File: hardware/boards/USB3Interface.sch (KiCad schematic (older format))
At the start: 5 parts, among them J2 USB3_Micro_B_Amphenol, U1 ECP5UM5G-381caBGA, U3 CYUSB3014

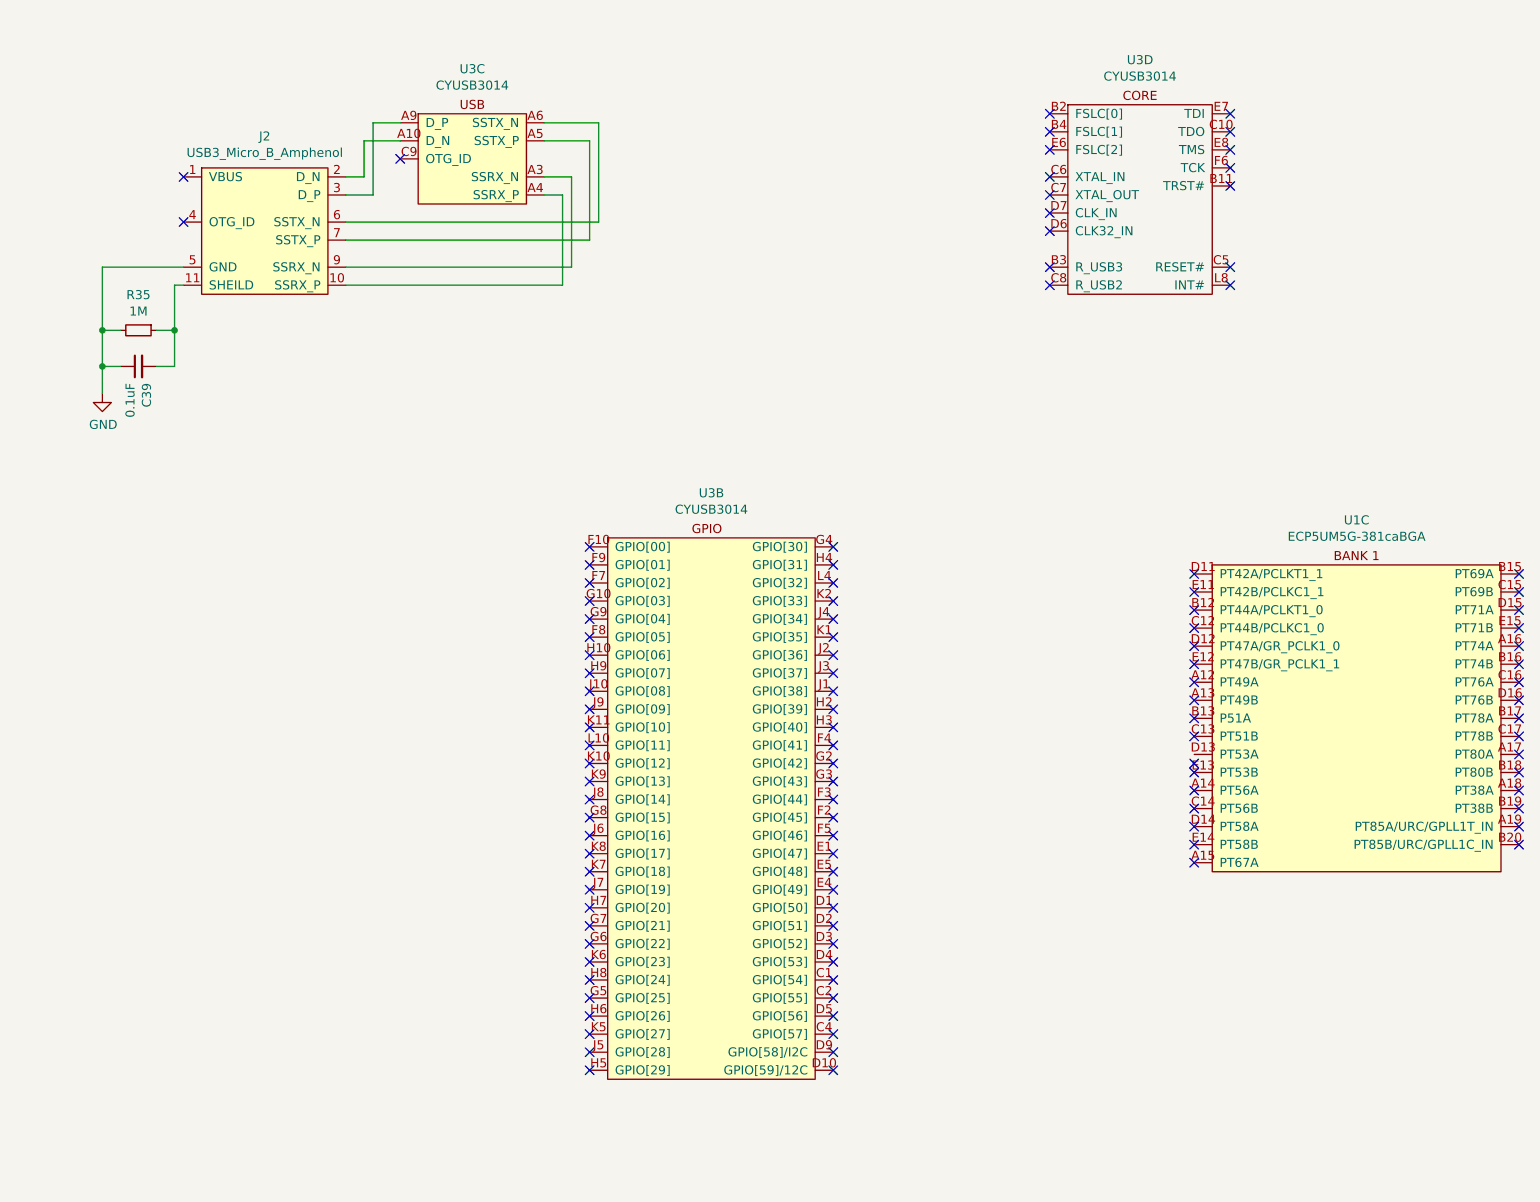
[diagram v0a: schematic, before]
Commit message: In an AHDH fuled stupor I made a bunch of changes, only the last of which I recall, which would be adding fiducials
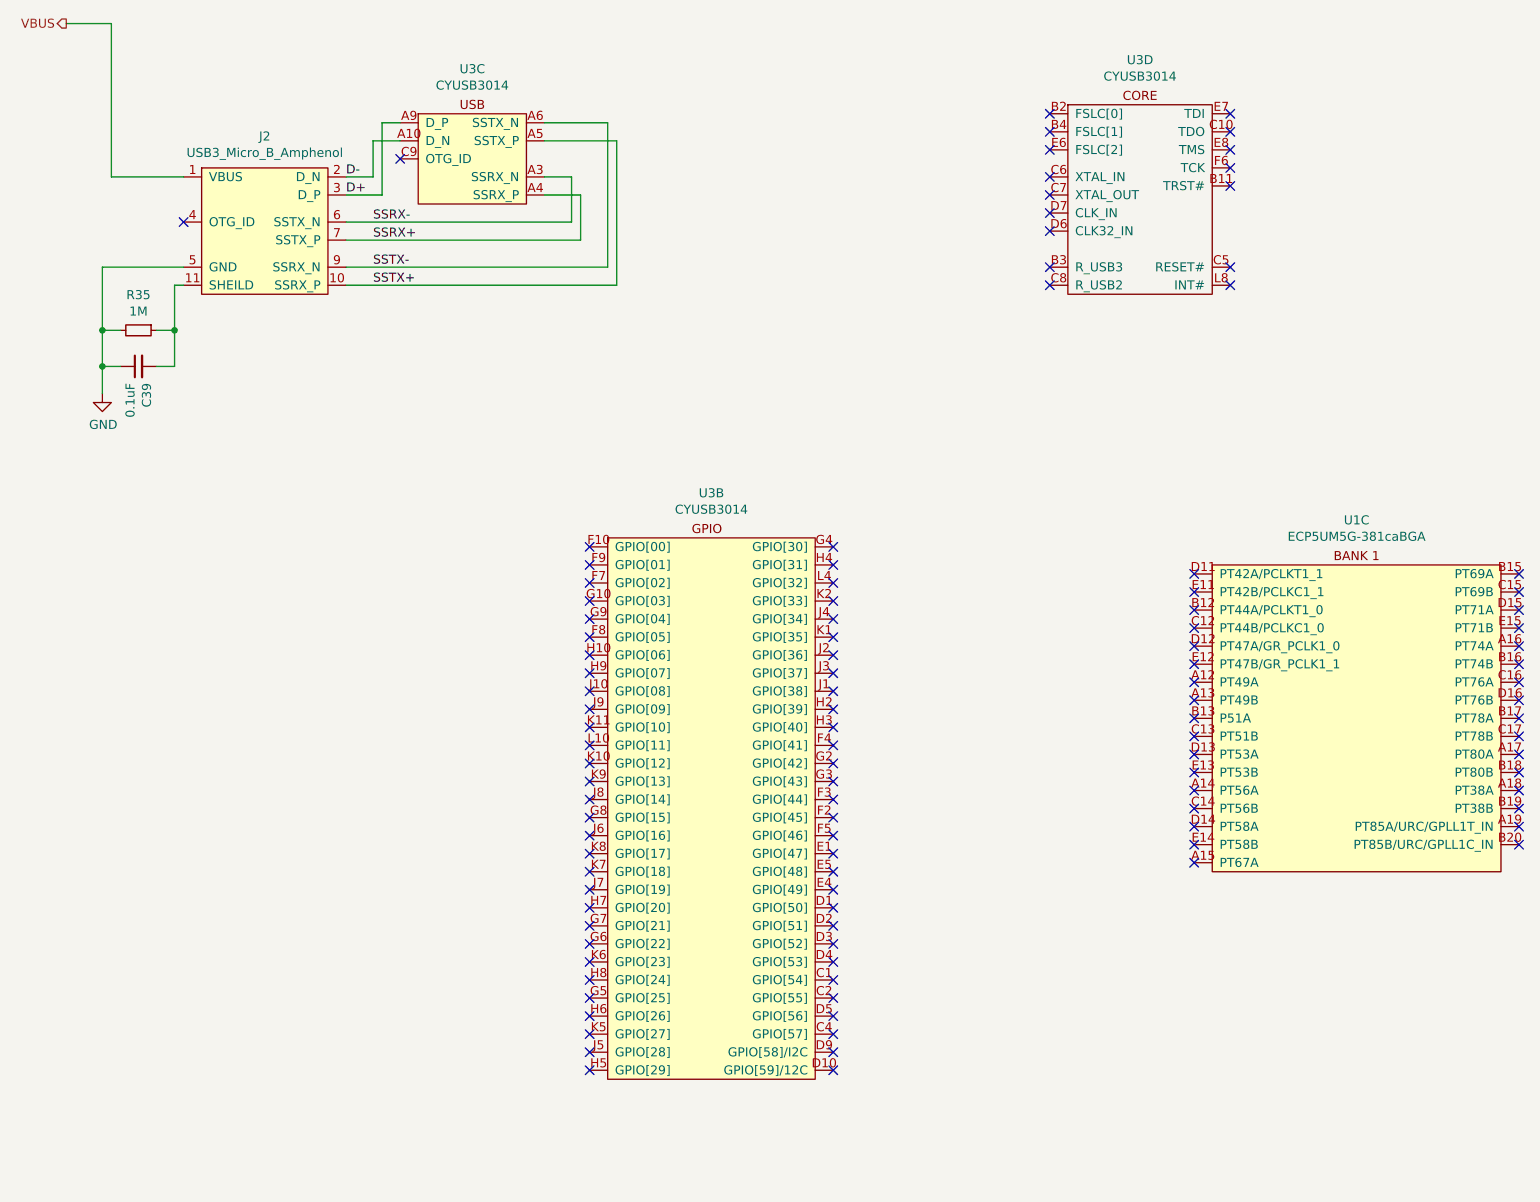
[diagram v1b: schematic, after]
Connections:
- net D-: now reaches J2.2 (D_N), U3.A10 (D_N)
- net SSRX-: now reaches U3.A3 (SSRX_N)
- net SSRX-: now also J2.6 (SSTX_N); no longer J2.9 (SSRX_N)
- net SSRX+: now reaches U3.A4 (SSRX_P)
- net SSRX+: now also J2.7 (SSTX_P); no longer J2.10 (SSRX_P)
- net SSTX+: now reaches U3.A5 (SSTX_P)
- net SSTX+: now also J2.10 (SSRX_P); no longer J2.7 (SSTX_P)
- net SSTX-: now reaches U3.A6 (SSTX_N)
- net SSTX-: now also J2.9 (SSRX_N); no longer J2.6 (SSTX_N)
- net D+: now reaches J2.3 (D_P), U3.A9 (D_P)
- net VBUS: now reaches J2.1 (VBUS)
- no-connect marks 112 -> 111
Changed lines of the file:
@@
 $EndComp
 Wire Wire Line
-	3450 1200 3750 1200
-Wire Wire Line
-	3750 1200 3750 1750
-Wire Wire Line
-	3750 1750 2350 1750
-Wire Wire Line
-	2350 1850 3700 1850
-Wire Wire Line
-	3700 1850 3700 1300
-Wire Wire Line
-	3700 1300 3450 1300
-Wire Wire Line
-	3450 1500 3600 1500
-Wire Wire Line
-	3600 1500 3600 2000
-Wire Wire Line
-	3600 2000 2350 2000
-Wire Wire Line
-	2350 1500 2450 1500
-Wire Wire Line
-	2450 1500 2450 1300
-Wire Wire Line
-	2450 1300 2650 1300
-Wire Wire Line
-	2350 1600 2500 1600
-Wire Wire Line
-	2500 1600 2500 1200
-Wire Wire Line
-	2500 1200 2650 1200
-Wire Wire Line
-	3450 1600 3550 1600
-Wire Wire Line
-	3550 1600 3550 2100
-Wire Wire Line
-	2350 2100 3550 2100
+	2350 1500 2500 1500
+Wire Wire Line
+	2500 1500 2500 1300
+Wire Wire Line
+	2500 1300 2650 1300
+Wire Wire Line
+	2350 1600 2550 1600
+Wire Wire Line
+	2550 1600 2550 1200
+Wire Wire Line
+	2550 1200 2650 1200
 $Comp
 L power:GND #PWR0118
@@
 	1400 2350 1400 2550
 NoConn ~ 1450 1750
-NoConn ~ 1450 1500
 NoConn ~ 2650 1400
 NoConn ~ 6250 1150
@@
 NoConn ~ 7050 4500
 NoConn ~ 7050 4600
-NoConn ~ 7050 4750
 NoConn ~ 7050 4800
 NoConn ~ 7050 4900
@@
 NoConn ~ 8850 3800
 NoConn ~ 8850 3700
+Text HLabel 800  650  0    50   Output ~ 0
+VBUS
+Wire Wire Line
+	1050 650  1050 1500
+Wire Wire Line
+	1050 1500 1450 1500
+Wire Wire Line
+	800  650  1050 650
+Wire Wire Line
+	2350 1750 3600 1750
+Wire Wire Line
+	3600 1750 3600 1500
+Wire Wire Line
+	3600 1500 3450 1500
+Wire Wire Line
+	2350 1850 3650 1850
+Wire Wire Line
+	3650 1850 3650 1600
+Wire Wire Line
+	3650 1600 3450 1600
+Wire Wire Line
+	2350 2000 3800 2000
+Wire Wire Line
+	3800 2000 3800 1200
+Wire Wire Line
+	3800 1200 3450 1200
+Wire Wire Line
+	2350 2100 3850 2100
+Wire Wire Line
+	3850 2100 3850 1300
+Wire Wire Line
+	3850 1300 3450 1300
+NoConn ~ 7050 4700
+Text Label 2500 1750 0    50   ~ 0
+SSRX-
+Text Label 2500 1850 0    50   ~ 0
+SSRX+
+Text Label 2500 2000 0    50   ~ 0
+SSTX-
+Text Label 2500 2100 0    50   ~ 0
+SSTX+
+Text Label 2350 1600 0    50   ~ 0
+D+
+Text Label 2350 1500 0    50   ~ 0
+D-
 $EndSCHEMATC

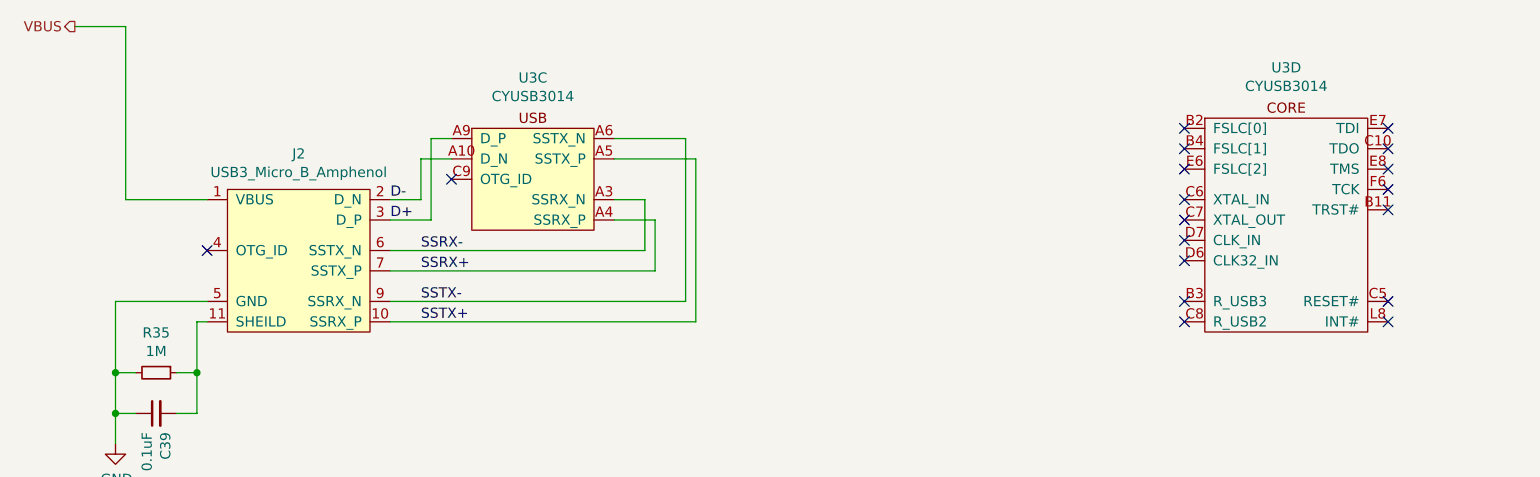
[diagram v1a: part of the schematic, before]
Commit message: Added the JTAG header and some misc cleanup
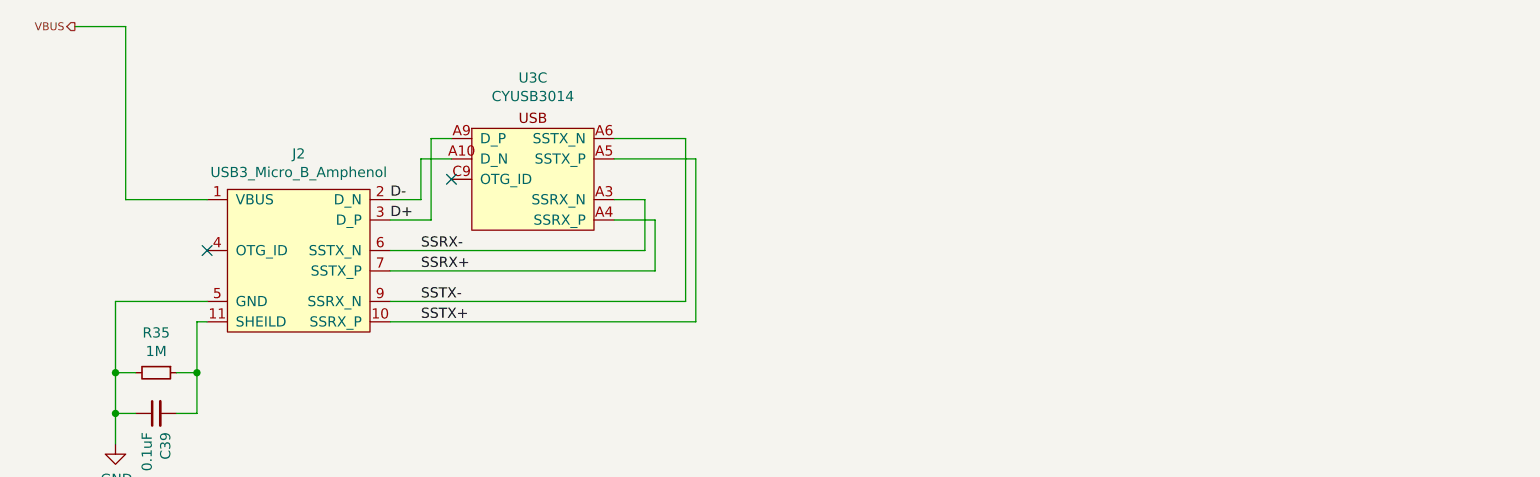
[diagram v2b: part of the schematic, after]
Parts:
- removed unit 4 of U3
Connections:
- no-connect marks 111 -> 95
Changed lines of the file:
@@
 $Descr A3 16535 11693
 encoding utf-8
-Sheet 3 11
+Sheet 2 11
 Title "lethallink"
 Date "2020-06-13"
@@
 $EndComp
 $Comp
-L lethalbit:CYUSB3014 U3
-U 4 1 5F335021
-P 6750 1650
-F 0 "U3" H 6750 2448 50  0000 C CNN
-F 1 "CYUSB3014" H 6750 2357 50  0000 C CNN
-F 2 "lethalbit:BGA-121_11x11_10.0x10.0mm" H 6750 2350 50  0001 C CNN
-F 3 "https://www.cypress.com/file/140296/download" H 6750 2350 50  0001 C CNN
-F 4 "Cypress" H 6750 1650 50  0001 C CNN "MFR"
-F 5 " CYUSB3014-BZXI" H 6750 1650 50  0001 C CNN "MPN"
-F 6 "428-3130-ND" H 6750 1650 50  0001 C CNN "DIGIKEY_PN"
-	4    6750 1650
-	1    0    0    -1
-$EndComp
-$Comp
 L lethalbit:USB3_Micro_B_Amphenol J2
 U 1 1 5F8A43B9
@@
 NoConn ~ 1450 1750
 NoConn ~ 2650 1400
-NoConn ~ 6250 1150
-NoConn ~ 6250 1250
-NoConn ~ 6250 1350
-NoConn ~ 6250 1500
-NoConn ~ 6250 1600
-NoConn ~ 6250 1700
-NoConn ~ 6250 1800
-NoConn ~ 6250 2000
-NoConn ~ 6250 2100
-NoConn ~ 7250 2100
-NoConn ~ 7250 2000
-NoConn ~ 7250 1550
-NoConn ~ 7250 1450
-NoConn ~ 7250 1350
-NoConn ~ 7250 1250
-NoConn ~ 7250 1150
 NoConn ~ 3700 3550
 NoConn ~ 3700 3650
@@
 NoConn ~ 8850 3800
 NoConn ~ 8850 3700
-Text HLabel 800  650  0    50   Output ~ 0
+Text HLabel 800  650  0    39   Output ~ 0
 VBUS
 Wire Wire Line

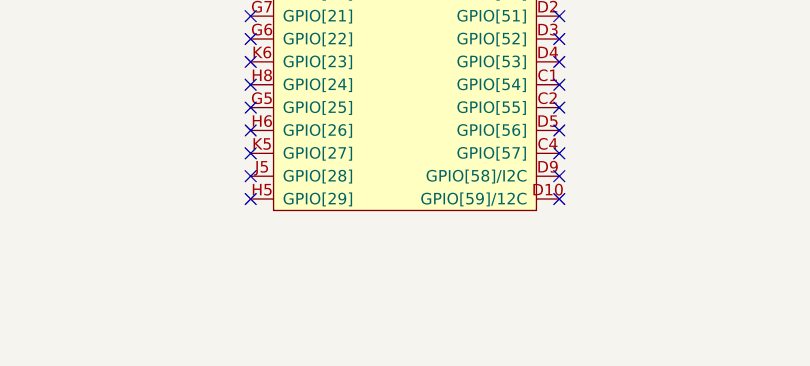
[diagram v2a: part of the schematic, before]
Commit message: Added a secondary SPI flash for the USB PHY Firmware. Yes it's overkill but it'll be fine. I'll use it to like, store configuration data or something
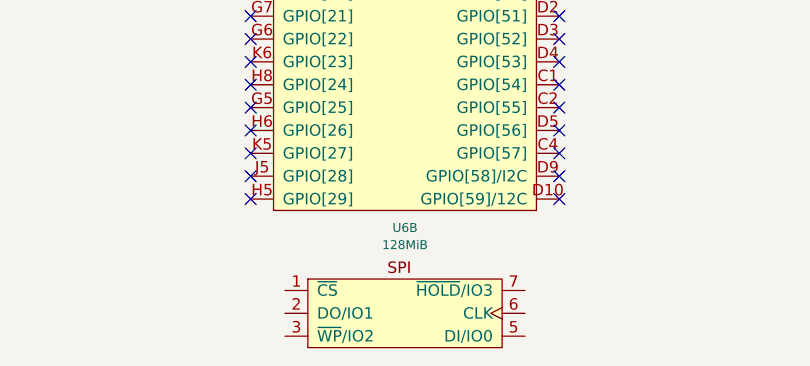
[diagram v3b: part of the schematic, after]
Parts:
- added U6: 128MiB, lethalbit-memory:WSON-8-1EP-6.0x8.0mm, symbol lethalbit-memory:W25N01GVZEIG
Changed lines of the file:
@@
 Text Label 2350 1500 0    50   ~ 0
 D-
+$Comp
+L lethalbit-memory:W25N01GVZEIG U?
+U 2 1 5FF1D42C
+P 4350 6800
+AR Path="/5EF66251/5FF1D42C" Ref="U?"  Part="2"
+AR Path="/5F2CAFD2/5FF1D42C" Ref="U6"  Part="2"
+F 0 "U6" H 4375 7024 39  0000 C CNN
+F 1 "128MiB" H 4375 6949 39  0000 C CNN
+F 2 "lethalbit-memory:WSON-8-1EP-6.0x8.0mm" H 4350 6950 39  0001 C CNN
+F 3 "https://www.winbond.com/resource-files/w25n01gv%20revl%20050918%20unsecured.pdf" H 4350 6950 39  0001 C CNN
+F 4 "Winbond" H 4350 6800 50  0001 C CNN "MFR"
+F 5 "W25N01GVZEIG" H 4350 6800 50  0001 C CNN "MPN"
+	2    4350 6800
+	1    0    0    -1
+$EndComp
 $EndSCHEMATC
